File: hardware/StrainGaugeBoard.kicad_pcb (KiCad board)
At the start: 2 copper layers, 108 parts, among them IC1 TCAN3413DR, IC2 LM74502DDFR, J1 SWD_Header, J10 CAN_OUT, J2 SWD, J4 CAN_DEBUG, J5 CAN_IN, Q1 PSMN012-100YS, Q2 PSMN012-100YS, SW1 Reset, SW2 SW_SPDT, U1 STM32G473CETx, U2 MCP1826S, U21 TS5A3166DBVR, U22 TS5A3166DBVR, U4 TPS2117DRLR, U5 TS5A3166DBVR, U6 ADS1220xPW, U7 ADS1220xPW, U8 TS5A3166DBVR, Y1 Crystal

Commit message: whoops forgot to push
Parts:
- removed C33: 0.1u, Capacitor_SMD:C_0603_1608Metric_Pad1.08x0.95mm_HandSolder
- removed C34: 4.7u, Capacitor_SMD:C_0805_2012Metric_Pad1.18x1.45mm_HandSolder
- removed C35: 100n, Capacitor_SMD:C_0603_1608Metric_Pad1.08x0.95mm_HandSolder
- removed C36: 100n, Capacitor_SMD:C_0603_1608Metric
- removed C37, C38: 22u, Capacitor_SMD:C_1210_3225Metric_Pad1.33x2.70mm_HandSolder
- removed C39: 3.3u, Capacitor_SMD:C_0805_2012Metric_Pad1.18x1.45mm_HandSolder
- removed D17, D18: LED, LED_SMD:LED_0603_1608Metric
- removed D8: TPD2EUSB30DRTR, LHRS_ICs:TPD2EUSB30DRTR
- removed D9: SMAF4758A, LHRS_Passives:SODFL5026X125N
- removed IC2: LM74502DDFR, LHRS_Power:LM74502DDFR
- removed Q1, Q2: PSMN012-100YS, Package_TO_SOT_SMD:LFPAK56
- removed R16, R18: 100k, Resistor_SMD:R_0603_1608Metric_Pad0.98x0.95mm_HandSolder
- removed R17: 7.32k, Resistor_SMD:R_0603_1608Metric_Pad0.98x0.95mm_HandSolder
- removed R19: 15.8k, Resistor_SMD:R_0603_1608Metric_Pad0.98x0.95mm_HandSolder
- removed R20: 100k, Resistor_SMD:R_0603_1608Metric
- removed R21: 19.1k, Resistor_SMD:R_0603_1608Metric
- removed TP1: V_in_12V, TestPoint:TestPoint_THTPad_D3.0mm_Drill1.5mm
- removed TP2: CB, TestPoint:TestPoint_THTPad_D3.0mm_Drill1.5mm
- removed TP3: FB, TestPoint:TestPoint_THTPad_D3.0mm_Drill1.5mm
- removed TP4: SW, TestPoint:TestPoint_THTPad_D3.0mm_Drill1.5mm
- removed TP_3.3V1: 3.3V, TestPoint:TestPoint_Loop_D1.80mm_Drill1.0mm_Beaded
- removed U21, U22, U8: TS5A3166DBVR, Package_TO_SOT_SMD:SOT-23-5
- removed U6, U7: ADS1220xPW, Package_SO:TSSOP-16_4.4x5mm_P0.65mm
- added C40: 1n, Capacitor_SMD:C_0603_1608Metric_Pad1.08x0.95mm_HandSolder, F.Cu at (83.3, 74.0)
- added C41: 1n, Capacitor_SMD:C_0603_1608Metric_Pad1.08x0.95mm_HandSolder, F.Cu at (83.3, 76.5)
- added C42: 220n, Capacitor_SMD:C_0603_1608Metric_Pad1.08x0.95mm_HandSolder, F.Cu at (83.3, 86.0)
- added C43: 10n, Capacitor_SMD:C_0603_1608Metric_Pad1.08x0.95mm_HandSolder, F.Cu at (83.3, 79.0)
- added C44: 1u, Capacitor_SMD:C_0603_1608Metric_Pad1.08x0.95mm_HandSolder, F.Cu at (83.3, 88.6)
- added C45: 0.1u, Capacitor_SMD:C_0603_1608Metric_Pad1.08x0.95mm_HandSolder, F.Cu at (83.3, 91.1)
- added C46: 1u, Capacitor_SMD:C_0603_1608Metric_Pad1.08x0.95mm_HandSolder, F.Cu at (83.3, 93.6)
- added C48: 0.1u, Capacitor_SMD:C_0603_1608Metric_Pad1.08x0.95mm_HandSolder, F.Cu at (83.3, 96.1)
- added C49: 0.1u, Capacitor_SMD:C_0603_1608Metric_Pad1.08x0.95mm_HandSolder, F.Cu at (181.1, 41.2)
- added C50: 1u, Capacitor_SMD:C_0603_1608Metric_Pad1.08x0.95mm_HandSolder, F.Cu at (184.7, 41.2)
- added C51: 220n, Capacitor_SMD:C_0603_1608Metric_Pad1.08x0.95mm_HandSolder, F.Cu at (191.5, 45.2)
- added C52: 10n, Capacitor_SMD:C_0603_1608Metric_Pad1.08x0.95mm_HandSolder, F.Cu at (201.0, 58.7)
- added C53: 10u, Capacitor_SMD:C_0805_2012Metric_Pad1.18x1.45mm_HandSolder, F.Cu at (184.5, 59.0)
- added C54: 1n, Capacitor_SMD:C_0603_1608Metric_Pad1.08x0.95mm_HandSolder, F.Cu at (64.7, 97.0)
- added C55: 1n, Capacitor_SMD:C_0603_1608Metric_Pad1.08x0.95mm_HandSolder, F.Cu at (64.7, 99.5)
- added C56: 10n, Capacitor_SMD:C_0603_1608Metric_Pad1.08x0.95mm_HandSolder, F.Cu at (64.7, 102.0)
- added C57: 0.1u, Capacitor_SMD:C_0603_1608Metric_Pad1.08x0.95mm_HandSolder, F.Cu at (185.0, 43.3)
- added C58: 0.1u, Capacitor_SMD:C_0603_1608Metric_Pad1.08x0.95mm_HandSolder, F.Cu at (189.8, 55.5)
- added C60: 1n, Capacitor_SMD:C_0603_1608Metric_Pad1.08x0.95mm_HandSolder, F.Cu at (64.7, 74.0)
- added C61: 1n, Capacitor_SMD:C_0603_1608Metric_Pad1.08x0.95mm_HandSolder, F.Cu at (64.7, 76.5)
- added C62: 10n, Capacitor_SMD:C_0603_1608Metric_Pad1.08x0.95mm_HandSolder, F.Cu at (64.7, 79.0)
- added C66: 1n, Capacitor_SMD:C_0603_1608Metric_Pad1.08x0.95mm_HandSolder, F.Cu at (41.3, 96.1)
- added C67: 1n, Capacitor_SMD:C_0603_1608Metric_Pad1.08x0.95mm_HandSolder, F.Cu at (41.3, 98.6)
- added C68: 0.1u, Capacitor_SMD:C_0603_1608Metric_Pad1.08x0.95mm_HandSolder, F.Cu at (83.3, 81.5)
- added C70: 0.1u, Capacitor_SMD:C_0603_1608Metric_Pad1.08x0.95mm_HandSolder, F.Cu at (64.7, 104.5)
- added C72: 0.1u, Capacitor_SMD:C_0603_1608Metric_Pad1.08x0.95mm_HandSolder, F.Cu at (64.7, 81.5)
- added C74: 10n, Capacitor_SMD:C_0603_1608Metric_Pad1.08x0.95mm_HandSolder, F.Cu at (41.3, 101.1)
- added C75: 0.1u, Capacitor_SMD:C_0603_1608Metric_Pad1.08x0.95mm_HandSolder, F.Cu at (41.3, 103.6)
- added CR1: D5V0P4UR6SO-7, LHRS_ICs:D5V0P4UR6SO-7, F.Cu at (75.9, 46.1)
- added D20: ESDA5V3SC5, Package_TO_SOT_SMD:SOT-23-5, F.Cu at (73.5, 64.2)
- added D22: ESDA5V3SC5, Package_TO_SOT_SMD:SOT-23-5, F.Cu at (54.7, 97.2)
- added F1: 1A, LHRS_Power:Fuse-3557-2, F.Cu at (176.7, 27.7)
- added IC3: LM74502DDFR, LHRS_Power:LM74502DDFR, F.Cu at (190.0, 52.2)
- added J11: Gauge, LHRS_Connectors:Molex_Nano-Fit_105309-xx02_1x02_P2.50mm_Vertical, F.Cu at (68.2, 89.0)
- added J13: Gauge, LHRS_Connectors:Molex_Nano-Fit_105309-xx02_1x02_P2.50mm_Vertical, F.Cu at (68.2, 66.0)
- added J15: Gauge A, LHRS_Connectors:Molex_Nano-Fit_105309-xx02_1x02_P2.50mm_Vertical, F.Cu at (44.7, 88.1)
- added J16: Gauge B, LHRS_Connectors:Molex_Nano-Fit_105309-xx02_1x02_P2.50mm_Vertical, F.Cu at (53.1, 88.1)
- added J3: SWD, Connector_PinHeader_2.54mm:PinHeader_1x04_P2.54mm_Vertical, F.Cu at (106.9, 44.8)
- added J6: Conn_01x06, Connector_PinHeader_2.54mm:PinHeader_1x06_P2.54mm_Vertical, F.Cu at (70.9, 38.2)
- added J8: Gauge, LHRS_Connectors:Molex_Nano-Fit_105309-xx02_1x02_P2.50mm_Vertical, F.Cu at (86.8, 66.0)
- added JP2: SolderJumper_2_Open, Jumper:SolderJumper-2_P1.3mm_Open_RoundedPad1.0x1.5mm, F.Cu at (180.8, 44.1)
- added Q3: PSMN012-100YS, Package_TO_SOT_SMD:LFPAK56, F.Cu at (176.4, 41.9)
- added Q4: PSMN012-100YS, Package_TO_SOT_SMD:LFPAK56, F.Cu at (176.3, 49.5)
- added R22: 1k, Resistor_SMD:R_0603_1608Metric_Pad0.98x0.95mm_HandSolder, F.Cu at (87.7, 74.0)
- added R23: 1k, Resistor_SMD:R_0603_1608Metric_Pad0.98x0.95mm_HandSolder, F.Cu at (87.7, 76.5)
- added R24: 350, Resistor_SMD:R_0603_1608Metric_Pad0.98x0.95mm_HandSolder, F.Cu at (87.7, 79.0)
- added R25: 350, Resistor_SMD:R_0603_1608Metric_Pad0.98x0.95mm_HandSolder, F.Cu at (87.7, 81.5)
- added R26: 350, Resistor_SMD:R_0603_1608Metric_Pad0.98x0.95mm_HandSolder, F.Cu at (92.0, 74.0)
- added R27: 350, Resistor_SMD:R_0603_1608Metric_Pad0.98x0.95mm_HandSolder, F.Cu at (92.0, 76.5)
- added R29: 1k, Resistor_SMD:R_0603_1608Metric_Pad0.98x0.95mm_HandSolder, F.Cu at (66.4, 37.2)
- added R35: 10k, Resistor_SMD:R_0603_1608Metric_Pad0.98x0.95mm_HandSolder, F.Cu at (185.0, 45.2)
- added R36: 33, Resistor_SMD:R_0603_1608Metric_Pad0.98x0.95mm_HandSolder, F.Cu at (205.3, 58.7)
- added R37: 1k, Resistor_SMD:R_0603_1608Metric_Pad0.98x0.95mm_HandSolder, F.Cu at (66.4, 39.7)
- added R38: 1k, Resistor_SMD:R_0603_1608Metric_Pad0.98x0.95mm_HandSolder, F.Cu at (69.1, 97.0)
- added R39: 1k, Resistor_SMD:R_0603_1608Metric_Pad0.98x0.95mm_HandSolder, F.Cu at (69.1, 99.5)
- added R40: 1k, Resistor_SMD:R_0603_1608Metric_Pad0.98x0.95mm_HandSolder, F.Cu at (66.4, 42.2)
- added R41: 22, Resistor_SMD:R_0603_1608Metric_Pad0.98x0.95mm_HandSolder, F.Cu at (66.4, 44.7)
- added R42: 22, Resistor_SMD:R_0603_1608Metric_Pad0.98x0.95mm_HandSolder, F.Cu at (66.4, 47.2)
- added R44: 350, Resistor_SMD:R_0603_1608Metric_Pad0.98x0.95mm_HandSolder, F.Cu at (69.1, 102.0)
- added R45: 350, Resistor_SMD:R_0603_1608Metric_Pad0.98x0.95mm_HandSolder, F.Cu at (69.1, 104.5)
- added R46: 350, Resistor_SMD:R_0603_1608Metric_Pad0.98x0.95mm_HandSolder, F.Cu at (73.4, 97.0)
- added R47: 350, Resistor_SMD:R_0603_1608Metric_Pad0.98x0.95mm_HandSolder, F.Cu at (73.4, 99.5)
- added R48: 22, Resistor_SMD:R_0603_1608Metric_Pad0.98x0.95mm_HandSolder, F.Cu at (66.4, 49.8)
- added R49: 100k, Resistor_SMD:R_0603_1608Metric_Pad0.98x0.95mm_HandSolder, F.Cu at (185.0, 47.2)
- added R50: 100k, Resistor_SMD:R_0603_1608Metric_Pad0.98x0.95mm_HandSolder, F.Cu at (92.0, 79.0)
- added R51: 7.32k, Resistor_SMD:R_0603_1608Metric_Pad0.98x0.95mm_HandSolder, F.Cu at (200.4, 52.2)
- added R52: 100k, Resistor_SMD:R_0603_1608Metric_Pad0.98x0.95mm_HandSolder, F.Cu at (73.4, 102.0)
- added R53: 100k, Resistor_SMD:R_0603_1608Metric_Pad0.98x0.95mm_HandSolder, F.Cu at (181.2, 54.2)
- added R54: 174k, Resistor_SMD:R_0603_1608Metric_Pad0.98x0.95mm_HandSolder, F.Cu at (92.0, 81.5)
- added R55: 15.8k, Resistor_SMD:R_0603_1608Metric_Pad0.98x0.95mm_HandSolder, F.Cu at (189.8, 57.2)
- added R56: 174k, Resistor_SMD:R_0603_1608Metric_Pad0.98x0.95mm_HandSolder, F.Cu at (73.4, 104.5)
- added R60: 0, Resistor_SMD:R_0603_1608Metric_Pad0.98x0.95mm_HandSolder, F.Cu at (66.4, 52.3)
- added R61: 10k, Resistor_SMD:R_0603_1608Metric_Pad0.98x0.95mm_HandSolder, F.Cu at (83.3, 98.6)
- added R62: 10k, Resistor_SMD:R_0603_1608Metric_Pad0.98x0.95mm_HandSolder, F.Cu at (83.3, 101.1)
- added R64: 16k, Resistor_SMD:R_0603_1608Metric_Pad0.98x0.95mm_HandSolder, F.Cu at (66.4, 54.8)
- added R65: 4.7k, Resistor_SMD:R_0603_1608Metric_Pad0.98x0.95mm_HandSolder, F.Cu at (66.4, 57.3)
- added R69: 1k, Resistor_SMD:R_0603_1608Metric_Pad0.98x0.95mm_HandSolder, F.Cu at (69.1, 74.0)
- added R70: 1k, Resistor_SMD:R_0603_1608Metric_Pad0.98x0.95mm_HandSolder, F.Cu at (69.1, 76.5)
- added R72: 174k, Resistor_SMD:R_0603_1608Metric_Pad0.98x0.95mm_HandSolder, F.Cu at (69.1, 79.0)
- added R73: 100k, Resistor_SMD:R_0603_1608Metric_Pad0.98x0.95mm_HandSolder, F.Cu at (69.1, 81.5)
- added R74: 350, Resistor_SMD:R_0603_1608Metric_Pad0.98x0.95mm_HandSolder, F.Cu at (73.4, 74.0)
- added R75: 350, Resistor_SMD:R_0603_1608Metric_Pad0.98x0.95mm_HandSolder, F.Cu at (73.4, 76.5)
- added R76: 350, Resistor_SMD:R_0603_1608Metric_Pad0.98x0.95mm_HandSolder, F.Cu at (73.4, 79.0)
- added R77: 350, Resistor_SMD:R_0603_1608Metric_Pad0.98x0.95mm_HandSolder, F.Cu at (73.4, 81.5)
- added R87: 1k, Resistor_SMD:R_0603_1608Metric_Pad0.98x0.95mm_HandSolder, F.Cu at (45.6, 96.1)
- added R88: 1k, Resistor_SMD:R_0603_1608Metric_Pad0.98x0.95mm_HandSolder, F.Cu at (45.6, 98.6)
- added R90: 174k, Resistor_SMD:R_0603_1608Metric_Pad0.98x0.95mm_HandSolder, F.Cu at (45.6, 101.1)
- added R91: 100k, Resistor_SMD:R_0603_1608Metric_Pad0.98x0.95mm_HandSolder, F.Cu at (45.6, 103.6)
- added R92: 350, Resistor_SMD:R_0603_1608Metric_Pad0.98x0.95mm_HandSolder, F.Cu at (50.0, 96.1)
- added R93: 350, Resistor_SMD:R_0603_1608Metric_Pad0.98x0.95mm_HandSolder, F.Cu at (50.0, 98.6)
- added R94: 350, Resistor_SMD:R_0603_1608Metric_Pad0.98x0.95mm_HandSolder, F.Cu at (50.0, 101.1)
- added R95: 350, Resistor_SMD:R_0603_1608Metric_Pad0.98x0.95mm_HandSolder, F.Cu at (50.0, 103.6)
- added TP17: Power TestPoint, TestPoint:TestPoint_Loop_D1.80mm_Drill1.0mm_Beaded, F.Cu at (41.4, 48.2)
- added TP18: MCU TestPoint, TestPoint:TestPoint_Loop_D1.80mm_Drill1.0mm_Beaded, F.Cu at (41.4, 52.8)
- added TP19: CAN TestPoint, TestPoint:TestPoint_Loop_D1.80mm_Drill1.0mm_Beaded, F.Cu at (41.4, 57.5)
- added TP20: +12V, TestPoint:TestPoint_Loop_D1.80mm_Drill1.0mm_Beaded, F.Cu at (46.1, 48.2)
- added TP21: +12V_PP, TestPoint:TestPoint_Loop_D1.80mm_Drill1.0mm_Beaded, F.Cu at (46.1, 52.8)
- added TP22: +5V_BUCK, TestPoint:TestPoint_Loop_D1.80mm_Drill1.0mm_Beaded, F.Cu at (46.1, 57.5)
- added TP23: +USBC_5V, TestPoint:TestPoint_Loop_D1.80mm_Drill1.0mm_Beaded, F.Cu at (50.7, 48.2)
- added TP24: MUX_OUT, TestPoint:TestPoint_Loop_D1.80mm_Drill1.0mm_Beaded, F.Cu at (50.7, 52.8)
- added TP25: LDO_OUT_TestPoint, TestPoint:TestPoint_Loop_D1.80mm_Drill1.0mm_Beaded, F.Cu at (50.7, 57.5)
- added TP29: SIG+, TestPoint:TestPoint_Pad_D1.5mm, F.Cu at (96.0, 74.5)
- added TP30: SIG+, TestPoint:TestPoint_Pad_D1.5mm, F.Cu at (77.4, 97.5)
- added TP31: SIG-, TestPoint:TestPoint_Pad_D1.5mm, F.Cu at (96.0, 78.1)
- added TP33: SIG-, TestPoint:TestPoint_Pad_D1.5mm, F.Cu at (77.4, 101.1)
- added TP36: SIG+, TestPoint:TestPoint_Pad_D1.5mm, F.Cu at (77.4, 74.5)
- added TP37: SIG-, TestPoint:TestPoint_Pad_D1.5mm, F.Cu at (77.4, 78.1)
- added TP40: SIG+, TestPoint:TestPoint_Pad_D1.5mm, F.Cu at (57.7, 85.7)
- added TP41: SIG-, TestPoint:TestPoint_Pad_D1.5mm, F.Cu at (57.7, 89.2)
- added TP5: VDDA, TestPoint:TestPoint_Loop_D1.80mm_Drill1.0mm_Beaded, F.Cu at (87.8, 95.2)
- added TP6: GNDA, TestPoint:TestPoint_Loop_D1.80mm_Drill1.0mm_Beaded, F.Cu at (87.8, 99.8)
- added U11: TS5A3166DBVR, Package_TO_SOT_SMD:SOT-23-5, F.Cu at (73.5, 91.8)
- added U13: TS5A3166DBVR, Package_TO_SOT_SMD:SOT-23-5, F.Cu at (73.5, 68.8)
- added U15: TS5A3166DBVR, Package_TO_SOT_SMD:SOT-23-5, F.Cu at (54.7, 101.9)
- added U3: TPS2117DRLR, LHRS_Power:TPS2117DRLR, F.Cu at (122.8, 63.6)
- added U9: ADS131M04xPW, Package_SO:TSSOP-20_4.4x6.5mm_P0.65mm, F.Cu at (90.2, 88.8)
- C1: value 26p -> 4.7u; footprint Capacitor_SMD:C_0603_1608Metric_Pad1.08x0.95mm_HandSolder -> Capacitor_SMD:C_0805_2012Metric_Pad1.18x1.45mm_HandSolder
- C10, C27, C28, C8: value 0.1uF -> 0.1u
- C11, C9: value 1uF -> 0.1u
- C12, C13: value 0.1uF -> 10u; footprint Capacitor_SMD:C_0603_1608Metric_Pad1.08x0.95mm_HandSolder -> Capacitor_SMD:C_0805_2012Metric_Pad1.18x1.45mm_HandSolder
- C14: value 0.1uF -> 26p
- C15: value 100nF -> 26p
- C16, C31: value 10u -> 0.1uF; footprint Capacitor_SMD:C_0805_2012Metric_Pad1.18x1.45mm_HandSolder -> Capacitor_SMD:C_0603_1608Metric_Pad1.08x0.95mm_HandSolder
- C17: value 0.1u -> 10uF; footprint Capacitor_SMD:C_0603_1608Metric_Pad1.08x0.95mm_HandSolder -> Capacitor_SMD:C_0805_2012Metric
- C18, C19, C22: value 0.1u -> 0.1uF
- C2: value 26p -> 100n
- C21: value 10u -> 0.1u; footprint Capacitor_SMD:C_0805_2012Metric_Pad1.18x1.45mm_HandSolder -> Capacitor_SMD:C_0603_1608Metric_Pad1.08x0.95mm_HandSolder
- C23: value 1u -> 0.1uF
- C24: value 10uF -> 1uF; footprint Capacitor_SMD:C_0805_2012Metric -> Capacitor_SMD:C_0603_1608Metric_Pad1.08x0.95mm_HandSolder
- C26: value 0.1uF -> 1uF
- C29: value 220n -> 0.1uF
- C3: value 0.1uF -> 100n; footprint Capacitor_SMD:C_0603_1608Metric_Pad1.08x0.95mm_HandSolder -> Capacitor_SMD:C_0603_1608Metric
- C30: value 10n -> 0.1uF
- C32: value 0.1u -> 100nF
- C4: value 10uF -> 22u; footprint Capacitor_SMD:C_0805_2012Metric -> Capacitor_SMD:C_1210_3225Metric_Pad1.33x2.70mm_HandSolder
- C5: value 0.1uF -> 22u; footprint Capacitor_SMD:C_0603_1608Metric_Pad1.08x0.95mm_HandSolder -> Capacitor_SMD:C_1210_3225Metric_Pad1.33x2.70mm_HandSolder
- C6: value 0.1uF -> 3.3u; footprint Capacitor_SMD:C_0603_1608Metric_Pad1.08x0.95mm_HandSolder -> Capacitor_SMD:C_0805_2012Metric_Pad1.18x1.45mm_HandSolder
- C7: value 0.1uF -> 10u; footprint Capacitor_SMD:C_0603_1608Metric_Pad1.08x0.95mm_HandSolder -> Capacitor_SMD:C_0805_2012Metric
- D1: value RGB_LED -> D_Schottky; footprint LHRS_Special:RGB_LED -> Diode_SMD:D_SOD-123
- D12: value ESDA5V3SC5 -> SMBJ15CA; footprint Package_TO_SOT_SMD:SOT-23-5 -> Diode_SMD:D_SMB
- D15: value ESDA5V3SC5 -> SMAF4758A; footprint Package_TO_SOT_SMD:SOT-23-5 -> LHRS_Passives:SODFL5026X125N
- D2: value TVS -> SP0503BAHT; footprint Diode_SMD:D_SOD-323 -> Package_TO_SOT_SMD:SOT-143
- D3: value LED -> SBA130CH-AU_R1_000A1; footprint LED_SMD:LED_0603_1608Metric -> Diode_SMD:D_SOD-323_HandSoldering
- D4: value CDSOT23-T24CAN -> RGB_LED; footprint LHRS_Passives:CDSOT23-T24CAN -> LHRS_Special:RGB_LED
- D5: value SBA130CH-AU_R1_000A1 -> CDSOT23-T24CAN; footprint Diode_SMD:D_SOD-323_HandSoldering -> LHRS_Passives:CDSOT23-T24CAN
- D6: value SMBJ15CA -> TVS; footprint Diode_SMD:D_SMB -> Diode_SMD:D_SOD-323
- D7: value D_Schottky -> LED; footprint Diode_SMD:D_SOD-123 -> LED_SMD:LED_0603_1608Metric
- J1: value SWD_Header -> USB_C_Receptacle_USB2.0_16P; footprint LHRS_Connectors:SWD_Conn -> LHRS_Connectors:USB_C_Receptacle_GCT_USB4105-xx-A_16P_TopMnt_Horizontal
- J2: value SWD -> SWD_Header; footprint Connector_PinHeader_2.54mm:PinHeader_1x04_P2.54mm_Vertical -> LHRS_Connectors:SWD_Conn
- J4: footprint Connector_Molex:Molex_Nano-Fit_105309-xx04_1x04_P2.50mm_Vertical -> LHRS_Connectors:Molex_Nano-Fit_105309-xx04_1x04_P2.50mm_Vertical
- L1: footprint LHRS_Passives:74439369082 -> LHRS_Power:XAL5050822MEC
- R1: value 1k -> 100k; footprint Resistor_SMD:R_0603_1608Metric_Pad0.98x0.95mm_HandSolder -> Resistor_SMD:R_0603_1608Metric
- R10: value 60 -> 22
- R11: value 5.1k -> 22
- R12: value 5.1k -> 10k
- R13: value 10k -> 60
- R14: value 10k -> 1k
- R15: value 33 -> 60
- R2: value 10k -> 19.1k; footprint Resistor_SMD:R_0603_1608Metric_Pad0.98x0.95mm_HandSolder -> Resistor_SMD:R_0603_1608Metric
- R3, R4: value 1k -> 5.1k
- R5: value 22 -> 10k
- R6: value 22 -> 1k
- R9: value 60 -> 1k
- U1: value STM32G473CETx -> LMR51635XDDCR; footprint LHRS_Special:48PinMCU -> LHRS_ICs:DDC0006A-MFG
- U2: value MCP1826S -> STM32G473CETx; footprint Package_TO_SOT_SMD:SOT-223-3_TabPin2 -> LHRS_Special:48PinMCU
- U4: value TPS2117DRLR -> MCP1826S; footprint LHRS_Power:TPS2117DRLR -> Package_TO_SOT_SMD:SOT-223-3_TabPin2
- moved D15 99.3 mm to (193.2, 48.2)
- moved C27 93.0 mm to (113.4, 31.2)
- moved C28 93.0 mm to (113.4, 33.7)
- moved R13 93.0 mm to (113.4, 36.2)
- moved D12 87.0 mm to (183.2, 50.8), turned to 180 degrees
- moved C24 85.5 mm to (87.1, 31.2)
- moved C21 84.4 mm to (113.4, 28.7)
- moved R12 80.1 mm to (95.8, 38.7)
- moved R11 80.1 mm to (95.8, 36.2)
- moved C25 79.4 mm to (87.1, 33.7)
- moved C26 79.4 mm to (87.1, 36.2)
- moved C20 73.5 mm to (122.5, 35.5)
- moved U4 73.0 mm to (116.1, 47.7)
- moved U2 70.5 mm to (86.6, 48.4)
- moved D5 70.3 mm to (122.5, 39.2)
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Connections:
- C1 pad 1: GND -> /+12V_PP
- C1 pad 2: Net-(U1-PF0-OSC_IN) -> GND
- C10 pad 1: +3.3V -> /Power_Mux/PR1
- C11 pad 1: /VDDA -> +5V
- C11 pad 2: GNDA -> GND
- C12 pad 1: +3.3V -> GND
- C12 pad 2: GND -> Net-(D3-K)
- C13 pad 1: +3.3V -> GND
- C13 pad 2: GND -> +3.3V
- C14 pad 1: +3.3V -> GND
- C14 pad 2: GND -> Net-(U2-PF0-OSC_IN)
- C15 pad 1: /VDDA -> Net-(U2-PF1-OSC_OUT)
- C15 pad 2: GNDA -> GND
- C16 pad 1: +3.3V -> /VDDA
- C16 pad 2: GND -> GNDA
- C18 pad 1: +3.3V -> /48PinMCU/NRST
- C19 pad 1: GND -> +3.3V
- C19 pad 2: Net-(C19-Pad2) -> GND
- C2 pad 1: Net-(U1-PF1-OSC_OUT) -> /+12V_PP
- C20 pad 1: GND -> +3.3V
- C20 pad 2: Net-(D5-K) -> GND
- C21 pad 1: GND -> +3.3V
- C21 pad 2: +3.3V -> GND
- C22 pad 1: /PowerProtection/Vin -> /VDDA
- C22 pad 2: GND -> GNDA
- C23 pad 1: GND -> +3.3V
- C23 pad 2: Net-(D9-K) -> GND
- C24 pad 1: GND -> /VDDA
- C24 pad 2: /+USBC_5V -> GNDA
- C25 pad 1: /+5V_BUCK -> +3.3V
- C26 pad 1: /+USBC_5V -> /VDDA
- C26 pad 2: GND -> GNDA
- C27 pad 1: /Power_Mux/PR1 -> +3.3V
- C28 pad 1: /MUX_OUT -> GND
- C28 pad 2: GND -> Net-(C28-Pad2)
- C29 pad 1: Net-(D9-K) -> +3.3V
- C29 pad 2: Net-(IC2-VCAP) -> GND
- C3 pad 1: /VDDA -> /12VBuck/CB
- C3 pad 2: GNDA -> /12VBuck/SW
- C30 pad 1: Net-(C30-Pad1) -> +3.3V
- C31 pad 1: /+12V_PP -> +3.3V
- C32 pad 1: /PowerProtection/OV -> /VDDA
- C32 pad 2: GND -> GNDA
- C4 pad 1: +3.3V -> /+5V_BUCK
- C5 pad 1: /48PinMCU/NRST -> /+5V_BUCK
- C6 pad 1: +3.3V -> /+5V_BUCK
- C7 pad 1: /VDDA -> GND
- C7 pad 2: GNDA -> /+USBC_5V
- C8 pad 1: +3.3V -> /+5V_BUCK
- C9 pad 1: /VDDA -> /+USBC_5V
- C9 pad 2: GNDA -> GND
- D1 pad 1: /48PinMCU/PA2 -> /+USBC_5V
- D1 pad 2: Net-(D1-Pad2) -> /USB-C_Connector/VBUS_IN
- D10 pad 3: /StrainGaugeChannel1/SIGA+ -> /StrainADC/StrainChannel0/SIG-
- D10 pad 4: /StrainGaugeChannel1/SIGA- -> /StrainADC/StrainChannel0/SIG+
- D12 pad 1: /VDDA -> GND
- D12 pad 2: GND -> /PowerProtection/Vin
- D14 pad 3: /StrainGaugeChannel1/SIGB+ -> /StrainADC/StrainChannel1/SIG-
- D14 pad 4: /StrainGaugeChannel1/SIGB- -> /StrainADC/StrainChannel1/SIG+
- D15 pad 1: /VDDA -> Net-(D15-K)
- D19 pad 1: unconnected-(D19-K-Pad1) -> GND
- D2 pad 2: Net-(D2-A2) -> /48PinMCU/USB_DP
- D3 pad 2: Net-(D2-A2) -> +5V
- D4 pad 1: /CAN_H -> /48PinMCU/PA2
- D4 pad 2: /CAN_L -> Net-(D4-Pad2)
- D4 pad 3: GND -> /48PinMCU/PA1
- D5 pad 1: Net-(D5-K) -> /CAN_H
- D5 pad 2: /MUX_OUT -> /CAN_L
- D6 pad 2: /PowerProtection/Vin -> Net-(D6-A2)
- D7 pad 1: /+USBC_5V -> Net-(D7-K)
- D7 pad 2: /USB-C_Connector/VBUS_IN -> Net-(D6-A2)
- J2 pad 3: Net-(J1-Pin_3) -> Net-(J2-Pin_3)
- J2 pad 4: Net-(J1-Pin_4) -> Net-(J2-Pin_4)
- R1 pad 1: Net-(D1-Pad2) -> /+5V_BUCK
- R1 pad 2: GND -> /12VBuck/FB
- R10 pad 1: Net-(C19-Pad2) -> /48PinMCU/SWCLK
- R10 pad 2: Net-(JP1-A) -> Net-(J2-Pin_3)
- R11 pad 1: GND -> /48PinMCU/SWDIO
- R11 pad 2: /USB-C_Connector/CC1 -> Net-(J2-Pin_4)
- R12 pad 1: GND -> /48PinMCU/BOOT0
- R12 pad 2: /USB-C_Connector/CC2 -> Net-(D6-A2)
- R13 pad 1: /+5V_BUCK -> /CAN_H
- R13 pad 2: Net-(U4-ST) -> Net-(C28-Pad2)
- R14 pad 1: Net-(D9-K) -> Net-(D7-K)
- R14 pad 2: /PowerProtection/Vin -> GND
- R15 pad 1: Net-(C30-Pad1) -> Net-(C28-Pad2)
- R15 pad 2: /PowerProtection/gate -> Net-(JP1-A)
- R2 pad 1: /48PinMCU/NRST -> /12VBuck/FB
- R2 pad 2: +3.3V -> GND
- R3 pad 1: Net-(D1-Pad4) -> GND
- R3 pad 2: GND -> /USB-C_Connector/CC1
- R4 pad 1: Net-(D1-Pad6) -> GND
- R4 pad 2: GND -> /USB-C_Connector/CC2
- R5 pad 1: /48PinMCU/SWCLK -> /+5V_BUCK
- R5 pad 2: Net-(J1-Pin_3) -> Net-(U3-ST)
- R6 pad 1: /48PinMCU/SWDIO -> Net-(D4-Pad2)
- R6 pad 2: Net-(J1-Pin_4) -> GND
- R7 pad 1: /48PinMCU/BOOT0 -> /48PinMCU/NRST
- R7 pad 2: Net-(D2-A2) -> +3.3V
- R8 pad 1: Net-(D3-K) -> Net-(D4-Pad4)
- R9 pad 1: /CAN_H -> Net-(D4-Pad6)
- R9 pad 2: Net-(C19-Pad2) -> GND
- SW2 pad 2: Net-(D2-A2) -> Net-(D6-A2)
- U1 pad 1: +3.3V -> /12VBuck/FB
- U1 pad 2: /48PinMCU/PC13 -> /+12V_PP
- U1 pad 3: /48PinMCU/PC14 -> /+12V_PP
- U1 pad 4: /48PinMCU/PC15 -> GND
- U1 pad 5: Net-(U1-PF0-OSC_IN) -> /12VBuck/SW
- U1 pad 6: Net-(U1-PF1-OSC_OUT) -> /12VBuck/CB
- U2 pad 1: Net-(D5-K) -> +3.3V
- U2 pad 2: GND -> /48PinMCU/PC13
- U2 pad 3: +3.3V -> /48PinMCU/PC14
- U4 pad 1: GND -> Net-(D3-K)
- U4 pad 2: /MUX_OUT -> GND
- U4 pad 3: /+5V_BUCK -> +3.3V
- U5 pad 2: /StrainGaugeChannel1/SIGA+ -> /StrainADC/StrainChannel0/SIG+
- U5 pad 4: /SHUNT_CAL1 -> /SHUNT_CAL0
- Y1 pad 1: Net-(U1-PF0-OSC_IN) -> Net-(U2-PF0-OSC_IN)
- Y1 pad 2: Net-(U1-PF1-OSC_OUT) -> Net-(U2-PF1-OSC_OUT)

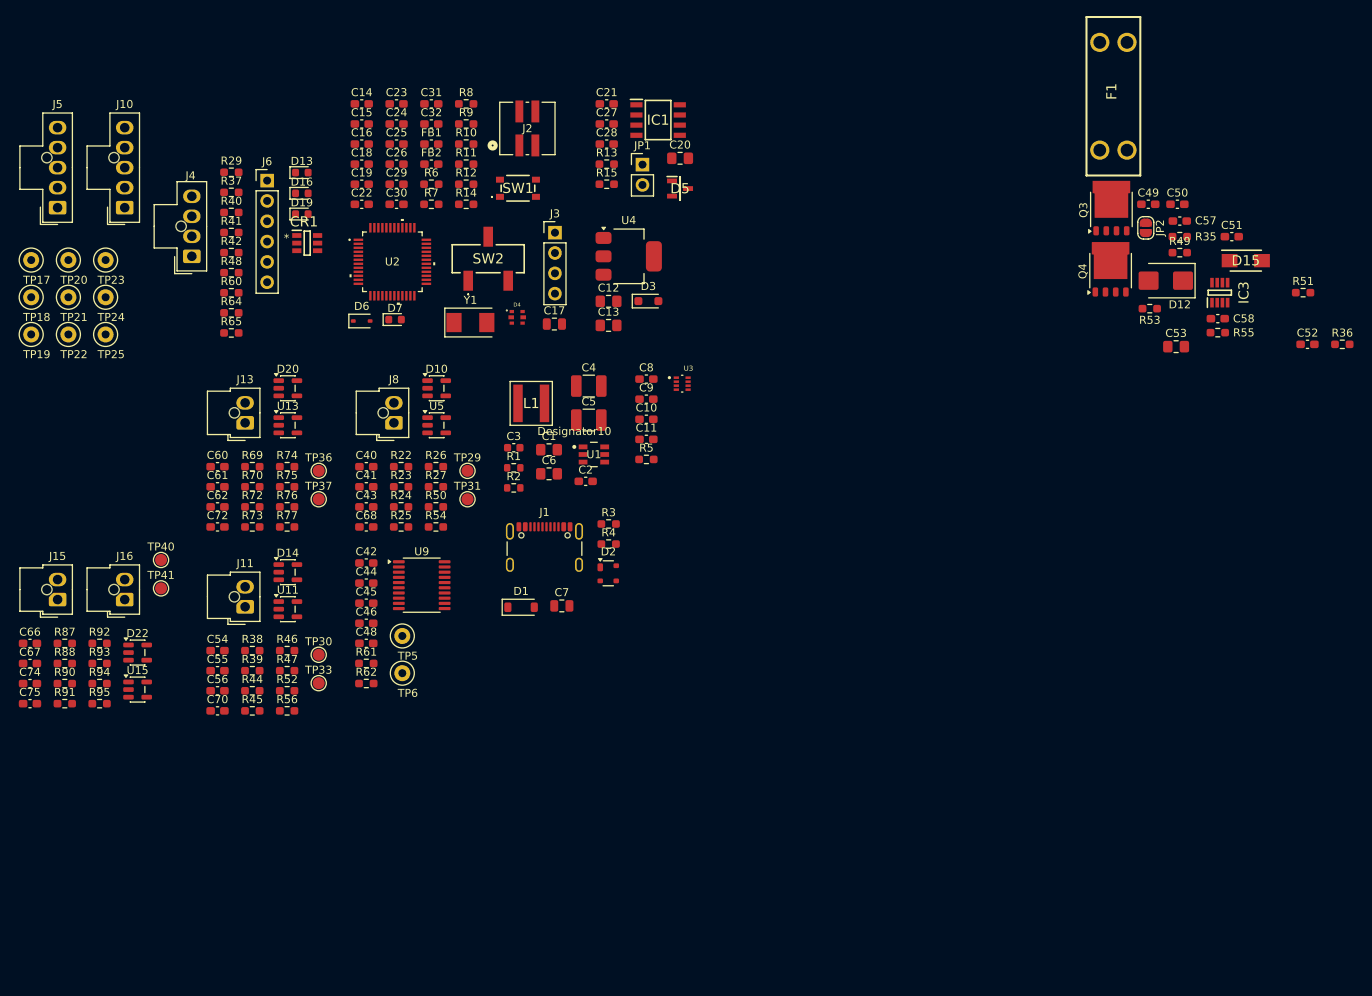
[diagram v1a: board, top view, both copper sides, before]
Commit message: Strain gauge board placement
- Power, MCU, USB and CAN blocks placed to match the BlackBody layout
- ADC centred under the MCU, four channel front-ends above their gauge connectors
- Gauge connectors updated to the schematic's Phoenix MSTBA 5.00 mm footprint, along the bottom edge
- Board outline 68.2 x 103 mm with 2 mm rounded corners, silkscreen labels
- Default clearance / hole clearance lowered to 0.15 mm
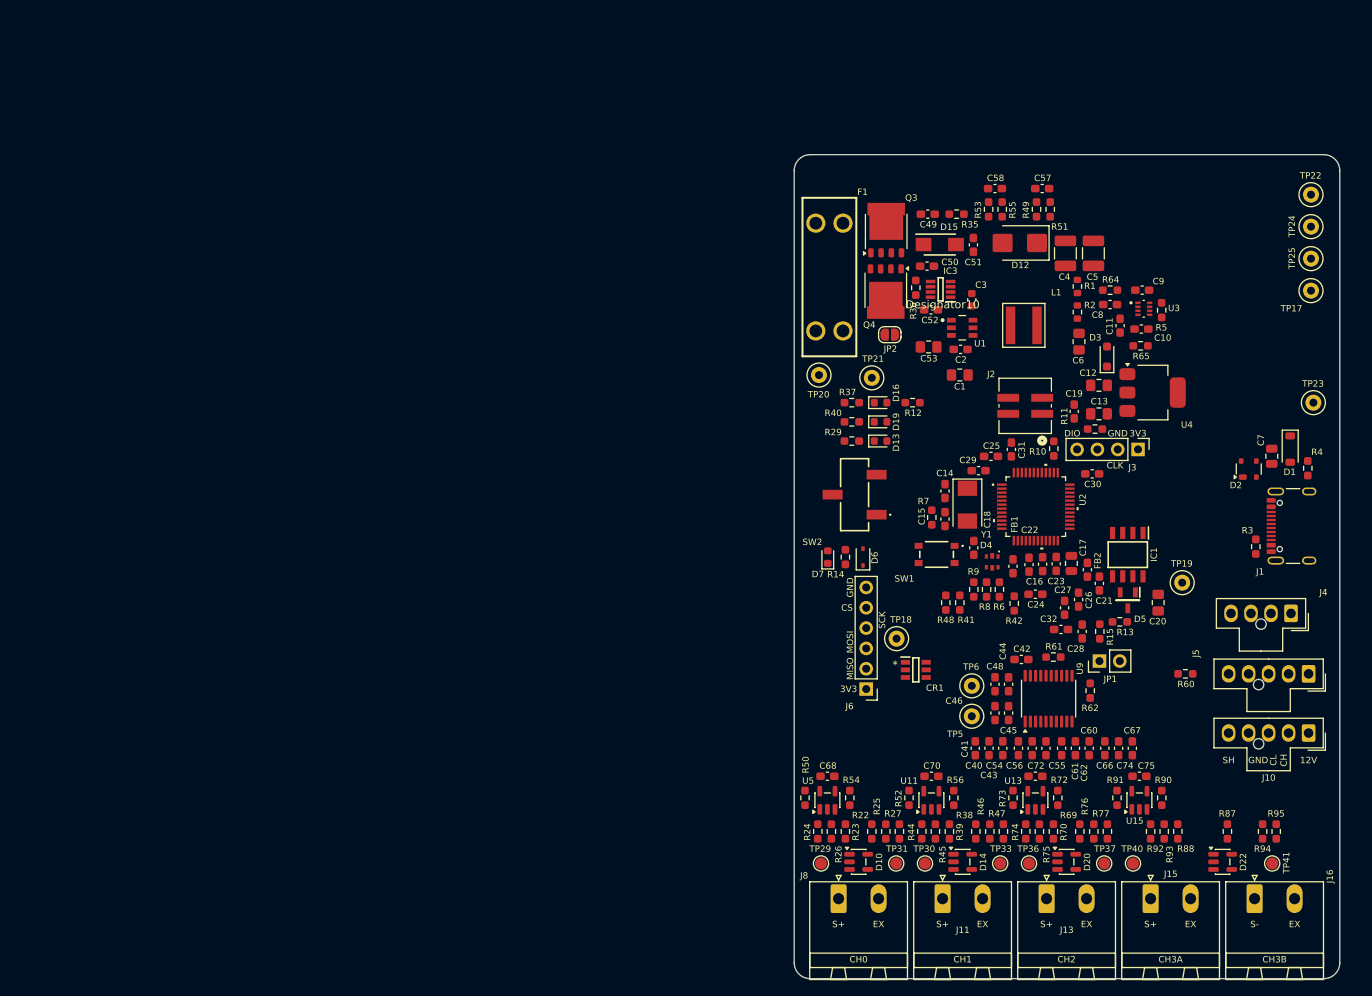
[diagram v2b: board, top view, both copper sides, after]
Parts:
- J11, J13, J15, J16, J8: footprint LHRS_Connectors:Molex_Nano-Fit_105309-xx02_1x02_P2.50mm_Vertical -> Connector_Phoenix_MSTB:PhoenixContact_MSTBA_2,5_2-G_1x02_P5.00mm_Horizontal
- moved J5 161.5 mm to (191.1, 99.9), turned to 90 degrees
- moved TP17 160.0 mm to (201.4, 52.0)
- moved J10 157.4 mm to (191.1, 107.3), turned to 90 degrees
- moved TP22 156.3 mm to (201.4, 40.0)
- moved TP23 152.0 mm to (201.7, 66.0)
- moved TP25 151.0 mm to (201.4, 48.0)
- moved TP24 150.9 mm to (201.4, 44.0)
- moved R95 147.9 mm to (197.1, 119.6), turned to 90 degrees
- moved R87 147.2 mm to (190.9, 119.6), turned to 90 degrees
- moved TP19 147.2 mm to (185.3, 88.5)
- moved J16 146.8 mm to (194.3, 128.0)
- moved R94 146.5 mm to (195.3, 119.6), turned to 90 degrees
- moved TP41 143.1 mm to (196.6, 123.6)
- moved J15 142.3 mm to (181.3, 128.0)
- moved J4 142.1 mm to (194.5, 92.6), turned to 90 degrees
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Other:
- board outline added: 68.2 x 103 mm
- board text added: "12V"
- board text added: "3V3"
- board text added: "CH"
- board text added: "CH0"
- board text added: "CH1"
- board text added: "CH2"
- board text added: "CH3A"
- board text added: "CH3B"
- board text added: "CL"
- board text added: "CLK"
- board text added: "CS"
- board text added: "DIO"
- board text added: "EX"
- board text added: "GND"
- board text added: "MISO"
- board text added: "MOSI"
- board text added: "S+"
- board text added: "S-"
- board text added: "SCK"
- board text added: "SH"
